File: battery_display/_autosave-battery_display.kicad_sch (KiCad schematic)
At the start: 20 parts, among them J1 FH34SRJ-24S-0.5SH_99_, Q1 ZXM61N03F, Q2 ZXM61N03F, SW1 Button-THT - 2-1825910-7

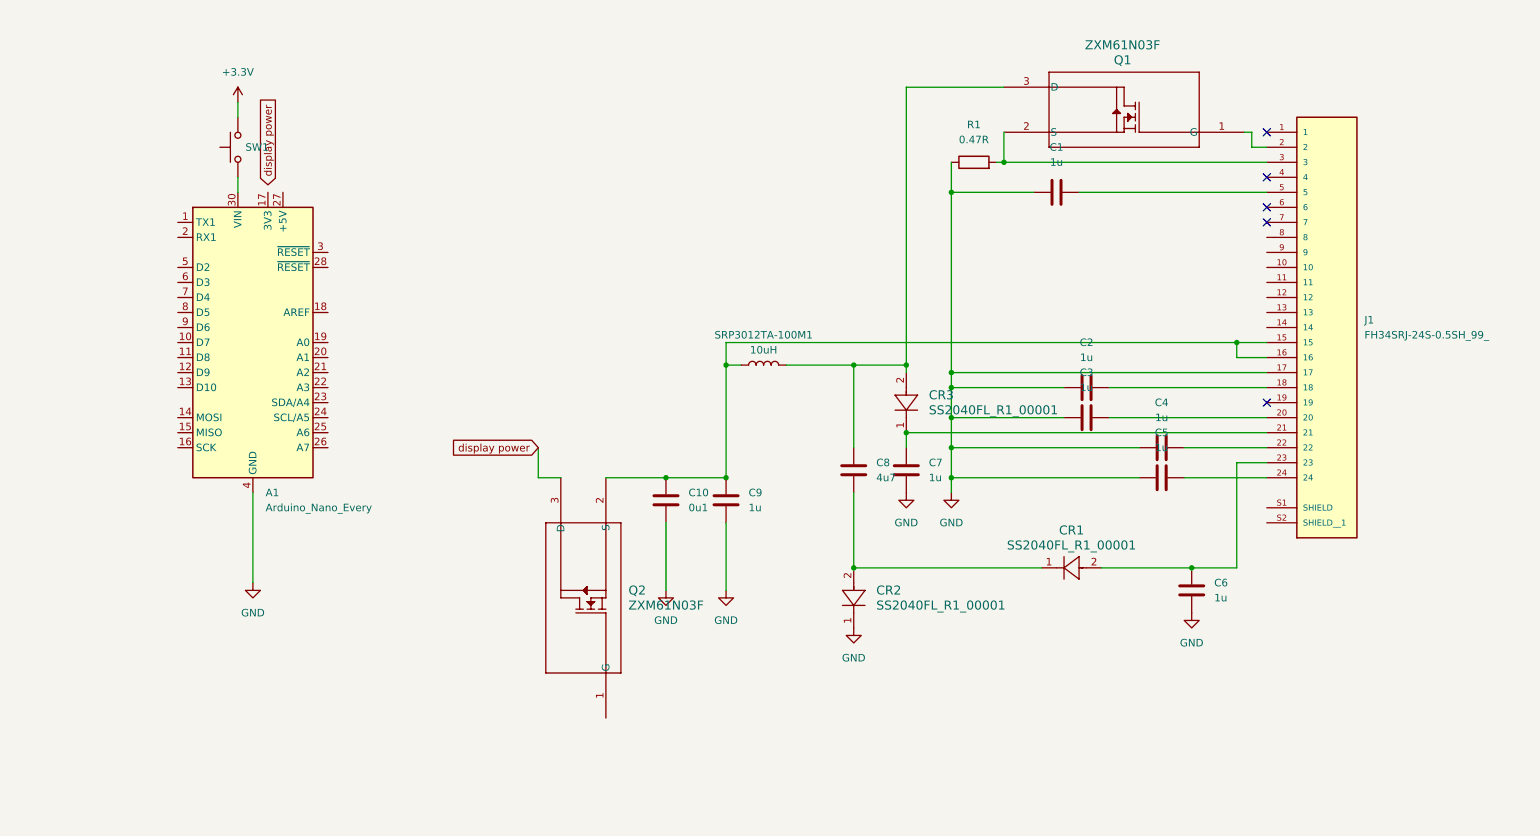
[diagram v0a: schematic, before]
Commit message: Schematic in progress
added base schematic
-next steps:
  -add connections to rpi pico
  -find values for soft start
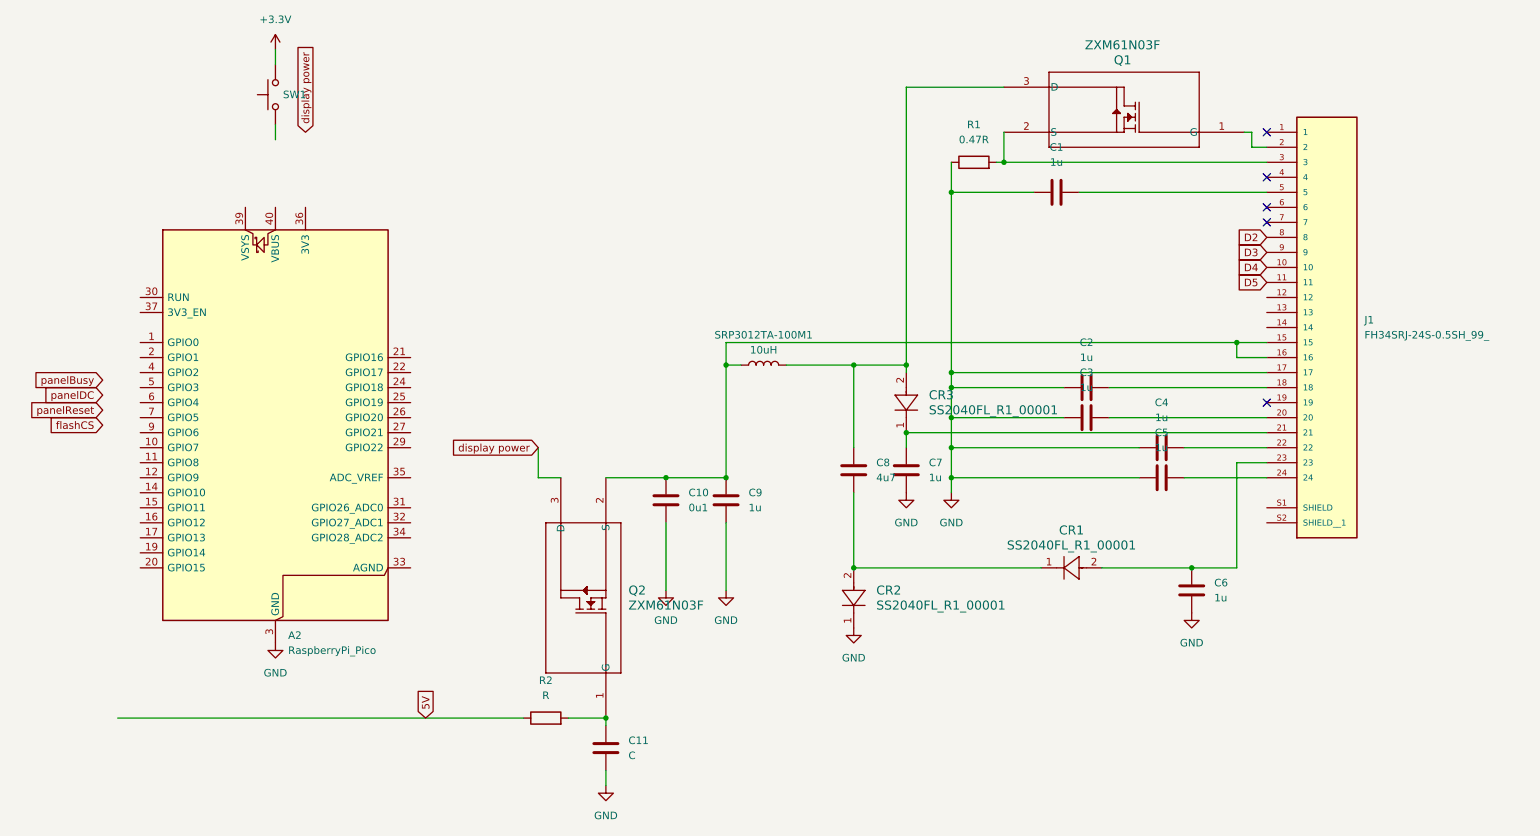
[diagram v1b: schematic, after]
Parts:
- removed A1: Arduino_Nano_Every, Module:Arduino_Nano, symbol MCU_Module:Arduino_Nano_Every
- added A2: RaspberryPi_Pico, Module:RaspberryPi_Pico_Common_Unspecified, symbol MCU_Module:RaspberryPi_Pico
- added C11: C, symbol Device:C
- added R2: R, symbol Device:R
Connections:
- net GND: now also A2.13 (GND), A2.18 (GND), A2.23 (GND), A2.28 (GND), A2.3 (GND), A2.38 (GND), A2.8 (GND), C11.2
- net D4: now reaches J1.10
- net D5: now reaches J1.11
- net D2: now reaches J1.8
- net D3: now reaches J1.9
- net at Q2.1 (G): now also C11.1, R2.2
- new net 5V: R2.1
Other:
- moved on the sheet: SW1
